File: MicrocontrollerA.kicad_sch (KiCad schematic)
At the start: 37 parts, among them J1 SWD Connector, J13 USB_B_Micro, SW1 SW_Push, SW2 SW_SPDT, SW3 SW_SPDT, U1 STM32F446RCTx, U5 TVS0500DRV, Y1 25 MHz

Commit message: Add interchangeable field to BOM
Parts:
- C1, C10, C11, C12, C2, C25, C3, C4, C5, C6, C7, C8, C9, D1, FB1, J13, R1, R10, R11, R2, R3, R4, R5, R6, R7, R8: Interchangeable (none) -> Yes
- D2, FL1, J1, SW1, SW2, SW3, U1, U5, Y1: Interchangeable (none) -> No
- TP4, TP5: Interchangeable (none) -> N/A

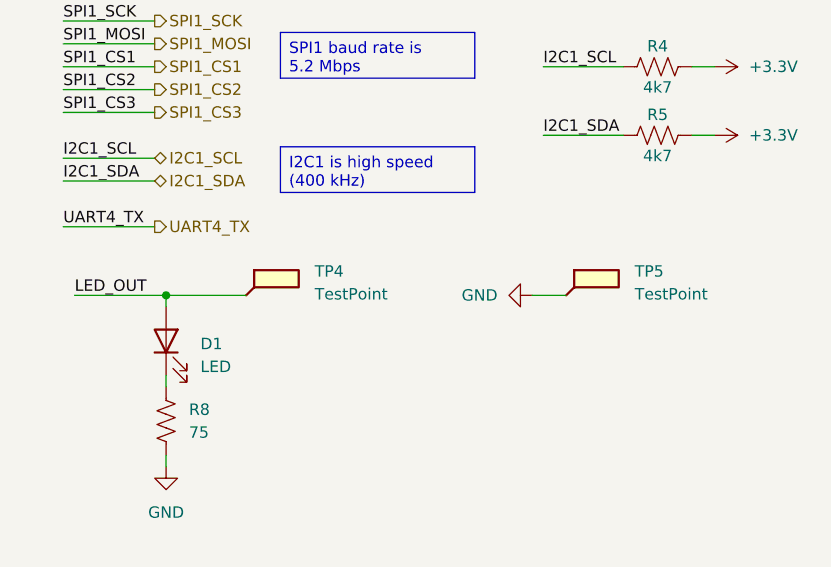
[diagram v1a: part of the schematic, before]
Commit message: Remove test points
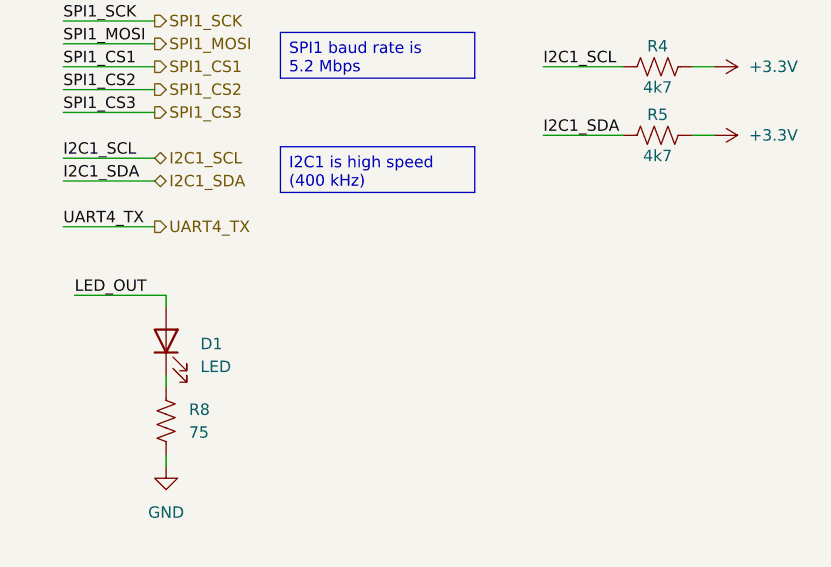
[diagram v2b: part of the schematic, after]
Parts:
- removed TP4, TP5: TestPoint, TestPoint:TestPoint_Plated_Hole_D2.0mm, symbol Connector:TestPoint_Flag
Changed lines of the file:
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@@
 	(title_block
 		(title "MCU A - STM32F446RCT6")
-		(date "2025-12-21")
-		(rev "A")
+		(date "2026-01-23")
+		(rev "B")
 		(company "CU Boulder Senior Design Team 29 - Xu Lab")
 	)
@@
 	)
 	(junction
-		(at 209.55 127)
-		(diameter 0)
-		(color 0 0 0 0)
-	)
-	(junction
 		(at 38.1 25.4)
 		(diameter 0)
@@
 	(wire
 		(pts
-			(xy 254 127) (xy 250.19 127)
-		)
-		(stroke
-			(width 0)
-			(type default)
-		)
-	)
-	(wire
-		(pts
 			(xy 119.38 26.67) (xy 119.38 25.4)
 		)
@@
 	(wire
 		(pts
-			(xy 209.55 127) (xy 218.44 127)
-		)
-		(stroke
-			(width 0)
-			(type default)
-		)
-	)
-	(wire
-		(pts
 			(xy 198.12 99.06) (xy 208.28 99.06)
 		)
@@
 	)
 	(symbol
-		(lib_id "Connector:TestPoint_Flag")
-		(at 218.44 127 0)
-		(unit 1)
-		(exclude_from_sim no)
-		(in_bom yes)
-		(on_board yes)
-		(dnp no)
-		(fields_autoplaced yes)
-		(property "Reference" "TP4"
-			(at 226.06 124.3329 0)
-			(effects
-				(font
-					(size 1.27 1.27)
-				)
-				(justify left)
-			)
-		)
-		(property "Value" "TestPoint"
-			(at 226.06 126.8729 0)
-			(effects
-				(font
-					(size 1.27 1.27)
-				)
-				(justify left)
-			)
-		)
-		(property "Footprint" "TestPoint:TestPoint_Plated_Hole_D2.0mm"
-			(at 223.52 127 0)
-			(effects
-				(font
-					(size 1.27 1.27)
-				)
-				(hide yes)
-			)
-		)
-		(property "Datasheet" ""
-			(at 223.52 127 0)
-			(effects
-				(font
-					(size 1.27 1.27)
-				)
-				(hide yes)
-			)
-		)
-		(property "Description" "test point (alternative flag-style design)"
-			(at 218.44 127 0)
-			(effects
-				(font
-					(size 1.27 1.27)
-				)
-				(hide yes)
-			)
-		)
-		(property "Interchangeable" "N/A"
-			(at 218.44 127 0)
-			(effects
-				(font
-					(size 1.27 1.27)
-				)
-				(hide yes)
-			)
-		)
-		(pin "1"
-		)
-		(instances
-			(project "XuLabPlatform"
-				(path "/71bb14ae-b730-4d22-a41d-cf68989dae2d/4b34bde8-cf26-4b12-b362-4972fe9ac1d6"
-					(reference "TP4")
-					(unit 1)
-				)
-			)
-		)
-	)
-	(symbol
 		(lib_id "power:+3.3V")
 		(at 25.4 22.86 0)
@@
 	)
 	(symbol
-		(lib_id "Connector:TestPoint_Flag")
-		(at 254 127 0)
-		(unit 1)
-		(exclude_from_sim no)
-		(in_bom yes)
-		(on_board yes)
-		(dnp no)
-		(fields_autoplaced yes)
-		(property "Reference" "TP5"
-			(at 261.62 124.3329 0)
-			(effects
-				(font
-					(size 1.27 1.27)
-				)
-				(justify left)
-			)
-		)
-		(property "Value" "TestPoint"
-			(at 261.62 126.8729 0)
-			(effects
-				(font
-					(size 1.27 1.27)
-				)
-				(justify left)
-			)
-		)
-		(property "Footprint" "TestPoint:TestPoint_Plated_Hole_D2.0mm"
-			(at 259.08 127 0)
-			(effects
-				(font
-					(size 1.27 1.27)
-				)
-				(hide yes)
-			)
-		)
-		(property "Datasheet" ""
-			(at 259.08 127 0)
-			(effects
-				(font
-					(size 1.27 1.27)
-				)
-				(hide yes)
-			)
-		)
-		(property "Description" "test point (alternative flag-style design)"
-			(at 254 127 0)
-			(effects
-				(font
-					(size 1.27 1.27)
-				)
-				(hide yes)
-			)
-		)
-		(property "Interchangeable" "N/A"
-			(at 254 127 0)
-			(effects
-				(font
-					(size 1.27 1.27)
-				)
-				(hide yes)
-			)
-		)
-		(pin "1"
-		)
-		(instances
-			(project "XuLabPlatform"
-				(path "/71bb14ae-b730-4d22-a41d-cf68989dae2d/4b34bde8-cf26-4b12-b362-4972fe9ac1d6"
-					(reference "TP5")
-					(unit 1)
-				)
-			)
-		)
-	)
-	(symbol
 		(lib_id "Device:C")
 		(at 63.5 30.48 0)
@@
 					(unit 1)
 				)
-			)
-		)
-	)
-	(symbol
-		(lib_id "power:GND")
-		(at 250.19 127 270)
-		(unit 1)
-		(exclude_from_sim no)
-		(in_bom yes)
-		(on_board yes)
-		(dnp no)
-		(fields_autoplaced yes)
-		(property "Reference" "#PWR057"
-			(at 243.84 127 0)
-			(effects
-				(font
-					(size 1.27 1.27)
-				)
-				(hide yes)
-			)
-		)
-		(property "Value" "GND"
-			(at 246.38 126.9999 90)
-			(effects
-				(font
-					(size 1.27 1.27)
-				)
-				(justify right)
-			)
-		)
-		(property "Footprint" ""
-			(at 250.19 127 0)
-			(effects
-				(font
-					(size 1.27 1.27)
-				)
-				(hide yes)
-			)
-		)
-		(property "Datasheet" ""
-			(at 250.19 127 0)
-			(effects
-				(font
-					(size 1.27 1.27)
-				)
-				(hide yes)
-			)
-		)
-		(property "Description" "Power symbol creates a global label with name \"GND\" , ground"
-			(at 250.19 127 0)
-			(effects
-				(font
-					(size 1.27 1.27)
-				)
-				(hide yes)
-			)
-		)
-		(pin "1"
-		)
-		(instances
-			(project "XuLabPlatform"
-				(path "/71bb14ae-b730-4d22-a41d-cf68989dae2d/4b34bde8-cf26-4b12-b362-4972fe9ac1d6"
-					(reference "#PWR057")
-					(unit 1)
-				)

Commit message: Change crystal capacitors to cheaper model
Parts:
- C11, C12: Listing https://www.digikey.com/en/products/detail/kyocera-avx/600L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 -> https://www.digikey.com/en/products/detail/yageo/CC0402JRNP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
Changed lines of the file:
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@@
 			)
 		)
-		(property "Datasheet" "https://datasheets.kyocera-avx.com/600L.pdf"
+		(property "Datasheet" "https://yageogroup.com/download/specsheet/CC0402JRNPO9BN220"
 			(at 59.69 184.15 0)
 			(effects
@@
 			)
 		)
-		(property "Listing" "https://www.digikey.com/en/products/detail/kyocera-avx/600L220JT200T4K/3905158"
+		(property "Listing" "https://www.digikey.com/en/products/detail/yageo/CC0402JRNPO9BN220/302752"
 			(at 59.69 184.15 0)
 			(effects
@@
 			)
 		)
-		(property "Datasheet" "https://datasheets.kyocera-avx.com/600L.pdf"
+		(property "Datasheet" "https://yageogroup.com/download/specsheet/CC0402JRNPO9BN220"
 			(at 34.29 184.15 0)
 			(effects
@@
 			)
 		)
-		(property "Listing" "https://www.digikey.com/en/products/detail/kyocera-avx/600L220JT200T4K/3905158"
+		(property "Listing" "https://www.digikey.com/en/products/detail/yageo/CC0402JRNPO9BN220/302752"
 			(at 34.29 184.15 0)
 			(effects

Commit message: Change SWD header to smaller footprint
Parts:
- J1: footprint Connector_IDC:IDC-Header_2x05_P2.54mm_Vertical -> Connector_PinHeader_1.27mm:PinHeader_2x05_P1.27mm_Vertical; Interchangeable No -> Yes; Listing https://www.digikey.com/en/products/detail/3m/N2510-6002-RB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 -> https://www.digikey.com/en/products/detail/sullins-connecto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
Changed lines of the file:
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@@
 	(title_block
 		(title "MCU A - STM32F446RCT6")
-		(date "2026-01-23")
+		(date "2026-01-25")
 		(rev "B")
 		(company "CU Boulder Senior Design Team 29 - Xu Lab")
@@
 			)
 		)
-		(property "Footprint" "Connector_IDC:IDC-Header_2x05_P2.54mm_Vertical"
+		(property "Footprint" "Connector_PinHeader_1.27mm:PinHeader_2x05_P1.27mm_Vertical"
 			(at 252.73 69.85 0)
 			(effects
@@
 			)
 		)
-		(property "Datasheet" "https://multimedia.3m.com/mws/media/330367O/3m-four-wall-header-2500-series-ts-0770.pdf"
+		(property "Datasheet" "https://s3.amazonaws.com/catalogspreads-pdf/PAGE94-95%20.050%20MALE%20HDR%20ST%20RA%20SMT.pdf"
 			(at 252.73 69.85 0)
 			(effects
@@
 			)
 		)
-		(property "Listing" "https://www.digikey.com/en/products/detail/3m/N2510-6002-RB/755176?msockid=2d45f8e4e5ba669a2195ea01e40967ef"
+		(property "Listing" "https://www.digikey.com/en/products/detail/sullins-connector-solutions/GRPB052VWVN-RC/1786455"
 			(at 252.73 69.85 0)
 			(effects
@@
 			)
 		)
-		(property "Interchangeable" "No"
+		(property "Interchangeable" "Yes"
 			(at 252.73 69.85 0)
 			(effects

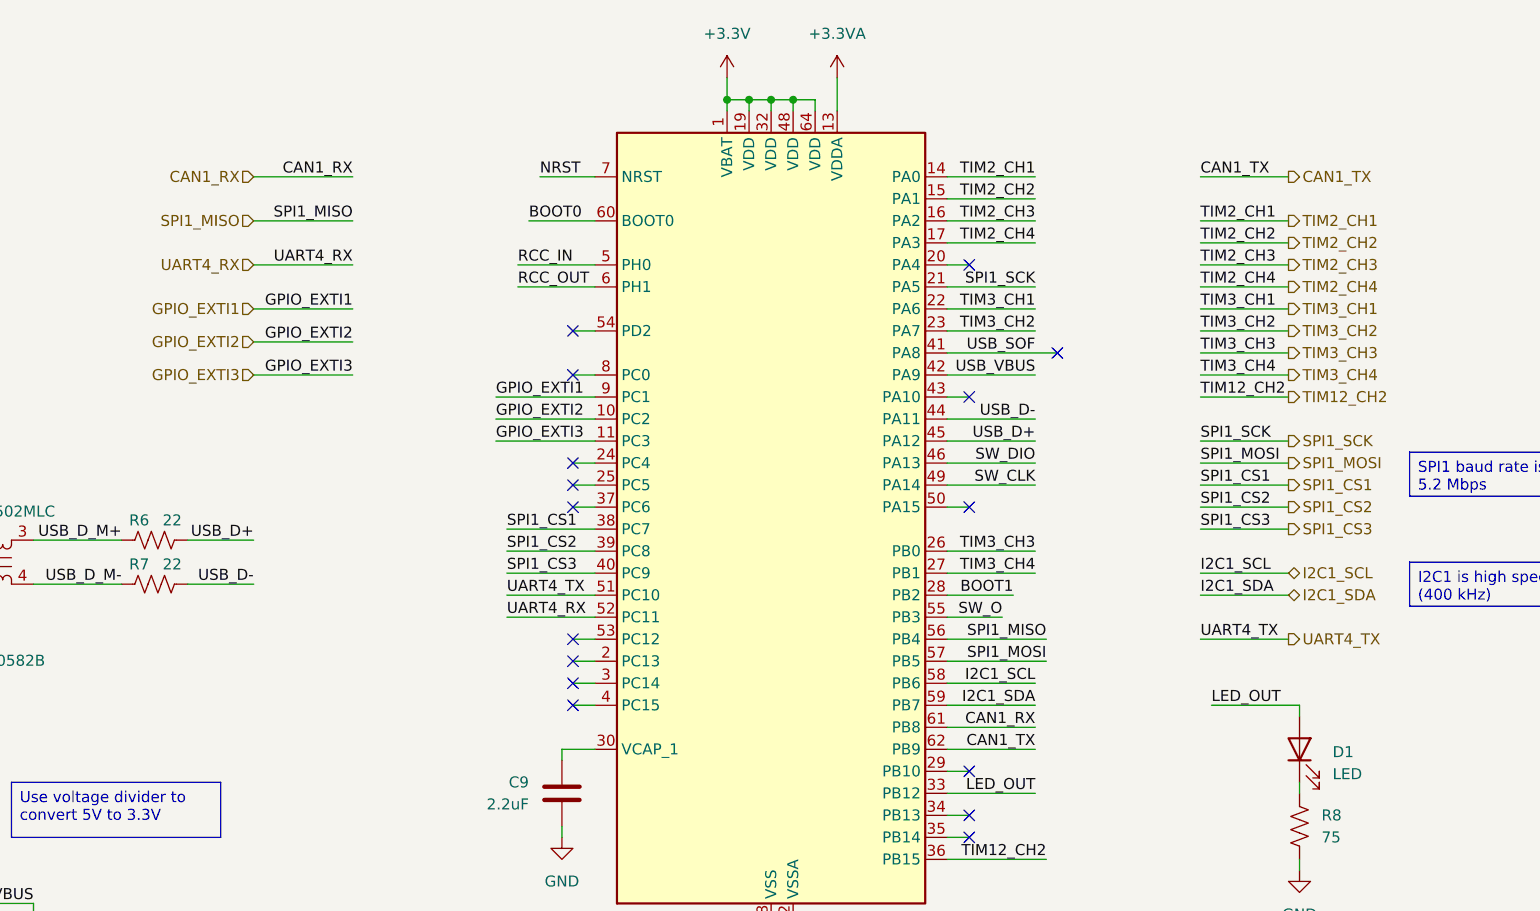
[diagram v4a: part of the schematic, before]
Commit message: Remove CAN pins and connector
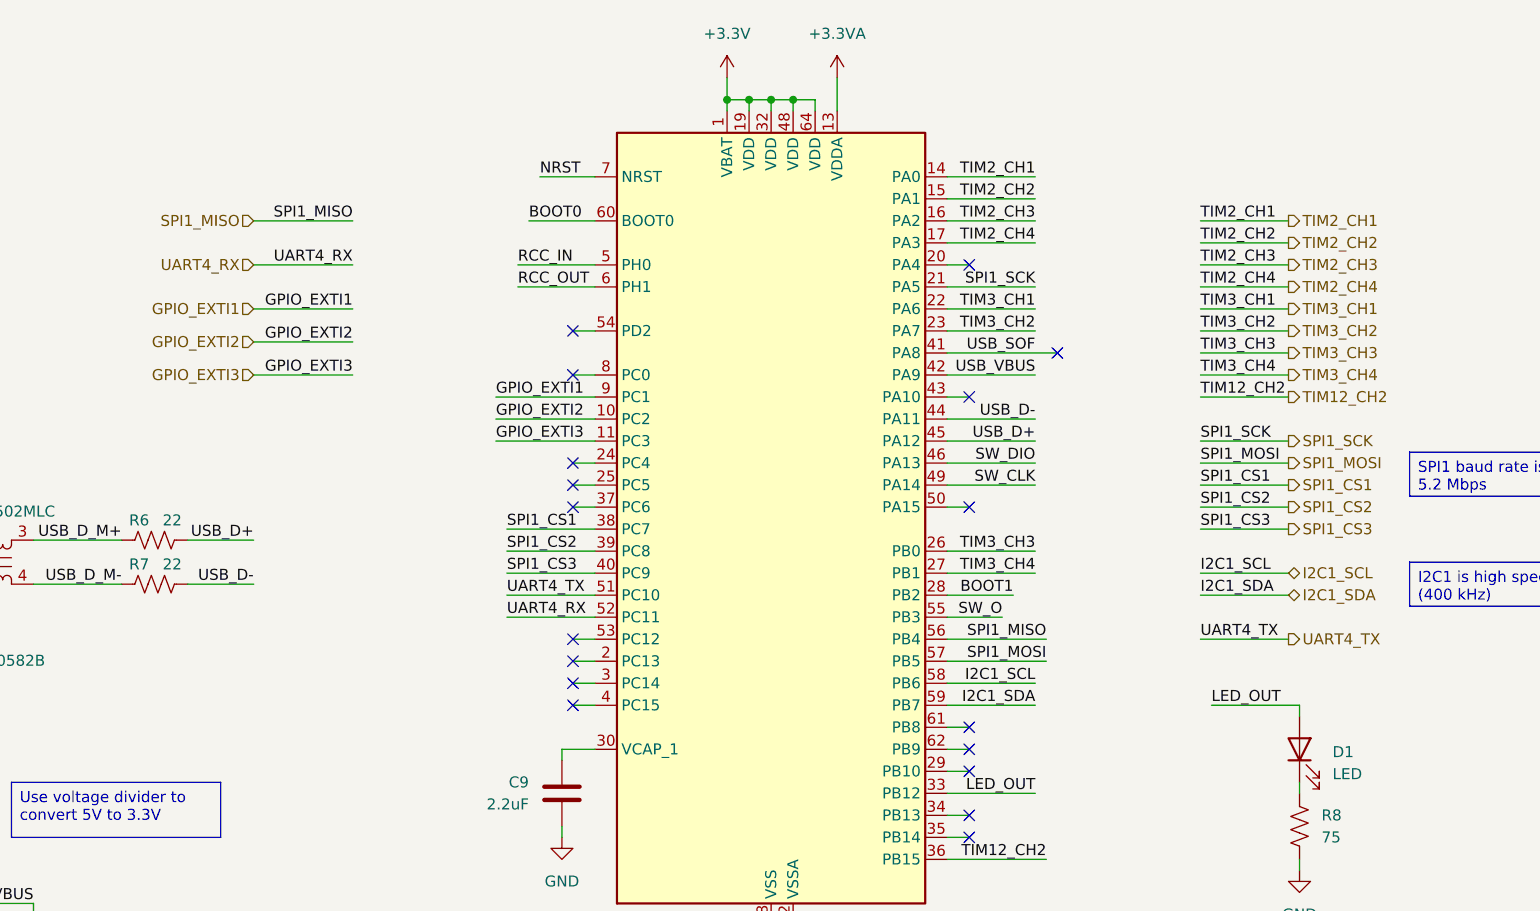
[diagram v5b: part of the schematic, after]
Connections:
- net CAN1_RX: no longer names the net of U1.61 (PB8)
- net CAN1_TX: no longer names the net of U1.62 (PB9)
- no-connect marks 19 -> 21
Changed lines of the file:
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@@
 	(title_block
 		(title "MCU A - STM32F446RCT6")
-		(date "2026-01-25")
+		(date "2026-01-27")
 		(rev "B")
 		(company "CU Boulder Senior Design Team 29 - Xu Lab")
@@
 	)
 	(no_connect
+		(at 171.45 129.54)
+	)
+	(no_connect
 		(at 171.45 91.44)
 	)
@@
 	)
 	(no_connect
+		(at 171.45 132.08)
+	)
+	(no_connect
 		(at 125.73 101.6)
 	)
@@
 	(wire
 		(pts
+			(xy 168.91 129.54) (xy 171.45 129.54)
+		)
+		(stroke
+			(width 0)
+			(type default)
+		)
+	)
+	(wire
+		(pts
 			(xy 81.28 107.95) (xy 88.9 107.95)
 		)
@@
 	(wire
 		(pts
+			(xy 168.91 132.08) (xy 171.45 132.08)
+		)
+		(stroke
+			(width 0)
+			(type default)
+		)
+	)
+	(wire
+		(pts
 			(xy 168.91 104.14) (xy 171.45 104.14)
 		)
@@
 	(wire
 		(pts
-			(xy 198.12 66.04) (xy 208.28 66.04)
-		)
-		(stroke
-			(width 0)
-			(type default)
-		)
-	)
-	(wire
-		(pts
 			(xy 148.59 152.4) (xy 148.59 153.67)
 		)
@@
 	(wire
 		(pts
-			(xy 168.91 132.08) (xy 179.07 132.08)
-		)
-		(stroke
-			(width 0)
-			(type default)
-		)
-	)
-	(wire
-		(pts
 			(xy 25.4 34.29) (xy 25.4 35.56)
 		)
@@
 	(wire
 		(pts
-			(xy 168.91 129.54) (xy 179.07 129.54)
-		)
-		(stroke
-			(width 0)
-			(type default)
-		)
-	)
-	(wire
-		(pts
 			(xy 146.05 57.15) (xy 148.59 57.15)
 		)
@@
 		(pts
 			(xy 39.37 114.3) (xy 38.1 114.3)
-		)
-		(stroke
-			(width 0)
-			(type default)
-		)
-	)
-	(wire
-		(pts
-			(xy 88.9 66.04) (xy 100.33 66.04)
 		)
 		(stroke
@@
 		)
 	)
-	(label "CAN1_TX"
-		(at 179.07 132.08 180)
-		(effects
-			(font
-				(size 1.27 1.27)
-			)
-			(justify right bottom)
-		)
-	)
 	(label "LED_OUT"
 		(at 179.07 137.16 180)
@@
 		)
 	)
-	(label "CAN1_RX"
-		(at 100.33 66.04 180)
-		(effects
-			(font
-				(size 1.27 1.27)
-			)
-			(justify right bottom)
-		)
-	)
-	(label "CAN1_TX"
-		(at 198.12 66.04 0)
-		(effects
-			(font
-				(size 1.27 1.27)
-			)
-			(justify left bottom)
-		)
-	)
 	(label "SW_O"
 		(at 175.26 116.84 180)
@@
 			)
 			(justify left bottom)
-		)
-	)
-	(label "CAN1_RX"
-		(at 179.07 129.54 180)
-		(effects
-			(font
-				(size 1.27 1.27)
-			)
-			(justify right bottom)
 		)
 	)
@@
 		)
 	)
-	(hierarchical_label "CAN1_RX"
-		(shape input)
-		(at 88.9 66.04 180)
-		(effects
-			(font
-				(size 1.27 1.27)
-			)
-			(justify right)
-		)
-	)
 	(hierarchical_label "I2C1_SDA"
 		(shape bidirectional)
@@
 		(effects
 			(font
-				(size 1.27 1.27)
-			)
-			(justify left)
-		)
-	)
-	(hierarchical_label "CAN1_TX"
-		(shape output)
-		(at 208.28 66.04 0)
-		(effects
-			(font

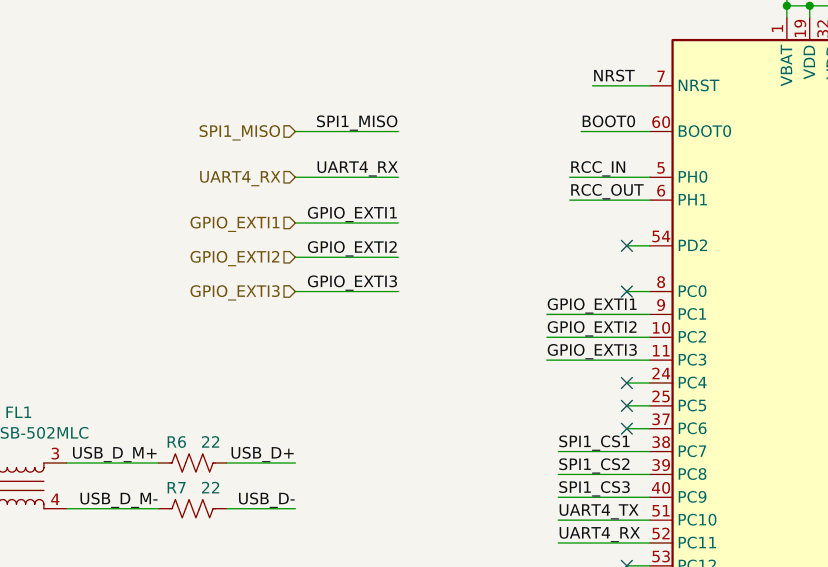
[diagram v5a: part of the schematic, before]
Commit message: Replace EXTI3 with EXTI0
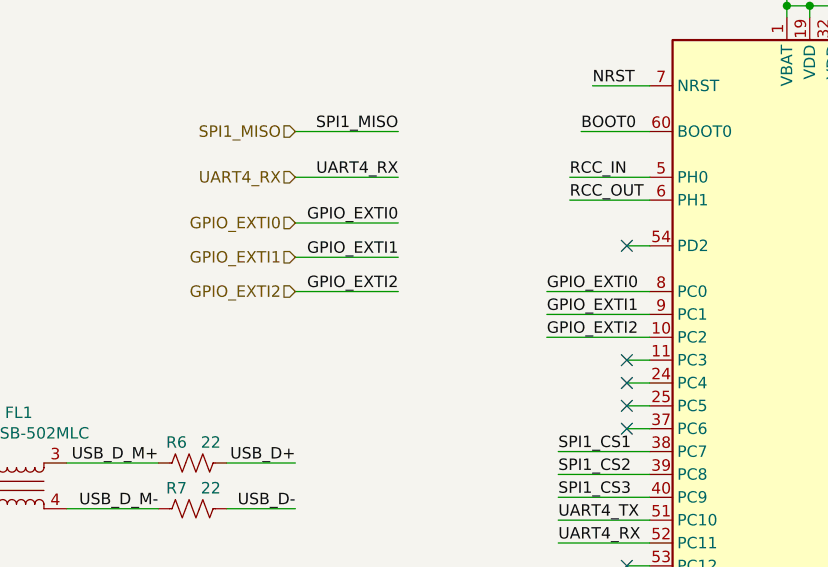
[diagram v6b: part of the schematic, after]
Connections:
- net GPIO_EXTI0: now reaches U1.8 (PC0)
- net GPIO_EXTI3: no longer names the net of U1.11 (PC3)
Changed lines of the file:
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@@
-	)
-	(no_connect
-		(at 125.73 88.9)
 	)
 	(no_connect
@@
 	)
 	(no_connect
+		(at 125.73 96.52)
+	)
+	(no_connect
 		(at 125.73 119.38)
 	)
@@
 	(wire
 		(pts
+			(xy 116.84 88.9) (xy 128.27 88.9)
+		)
+		(stroke
+			(width 0)
+			(type default)
+		)
+	)
+	(wire
+		(pts
 			(xy 243.84 63.5) (xy 243.84 64.77)
 		)
@@
 	(wire
 		(pts
+			(xy 125.73 96.52) (xy 128.27 96.52)
+		)
+		(stroke
+			(width 0)
+			(type default)
+		)
+	)
+	(wire
+		(pts
 			(xy 88.9 88.9) (xy 100.33 88.9)
 		)
@@
 	(wire
 		(pts
-			(xy 116.84 96.52) (xy 128.27 96.52)
-		)
-		(stroke
-			(width 0)
-			(type default)
-		)
-	)
-	(wire
-		(pts
 			(xy 125.73 83.82) (xy 128.27 83.82)
 		)
@@
 		(pts
 			(xy 38.1 63.5) (xy 38.1 64.77)
-		)
-		(stroke
-			(width 0)
-			(type default)
-		)
-	)
-	(wire
-		(pts
-			(xy 125.73 88.9) (xy 128.27 88.9)
 		)
 		(stroke
@@
 		)
 	)
-	(label "GPIO_EXTI3"
-		(at 116.84 96.52 0)
-		(effects
-			(font
-				(size 1.27 1.27)
-			)
-			(justify left bottom)
-		)
-	)
-	(label "GPIO_EXTI3"
+	(label "GPIO_EXTI2"
 		(at 100.33 88.9 180)
 		(effects
@@
 		)
 	)
+	(label "GPIO_EXTI0"
+		(at 116.84 88.9 0)
+		(effects
+			(font
+				(size 1.27 1.27)
+			)
+			(justify left bottom)
+		)
+	)
 	(label "TIM2_CH4"
 		(at 179.07 73.66 180)
@@
 		)
 	)
-	(label "GPIO_EXTI1"
+	(label "GPIO_EXTI0"
 		(at 100.33 81.28 180)
 		(effects
@@
 		)
 	)
-	(label "GPIO_EXTI2"
+	(label "GPIO_EXTI1"
 		(at 100.33 85.09 180)
 		(effects
@@
 		)
 	)
-	(hierarchical_label "GPIO_EXTI2"
+	(hierarchical_label "GPIO_EXTI1"
 		(shape input)
 		(at 88.9 85.09 180)
@@
 		)
 	)
-	(hierarchical_label "GPIO_EXTI3"
+	(hierarchical_label "GPIO_EXTI2"
 		(shape input)
 		(at 88.9 88.9 180)
@@
 		)
 	)
-	(hierarchical_label "GPIO_EXTI1"
+	(hierarchical_label "GPIO_EXTI0"
 		(shape input)
 		(at 88.9 81.28 180)
